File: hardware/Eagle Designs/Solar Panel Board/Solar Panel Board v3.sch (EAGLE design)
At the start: 44 parts, among them J1 MOLEX_503763-0291MOLEX_503763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, J2 MOLEX_503763-0491MOLEX_503763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, J3 MOLEX_503763-0291MOLEX_503763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, U1 TMP36GSZ, U2 INA219BIDR

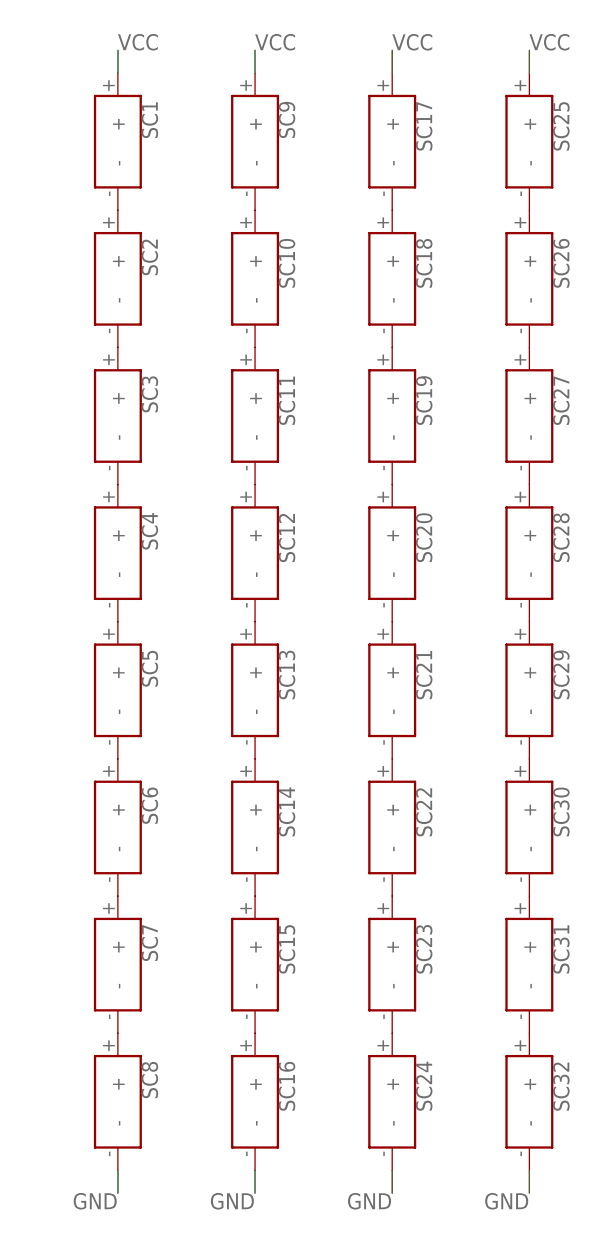
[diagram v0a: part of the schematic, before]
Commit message: Updated antenna and solar panel boards.
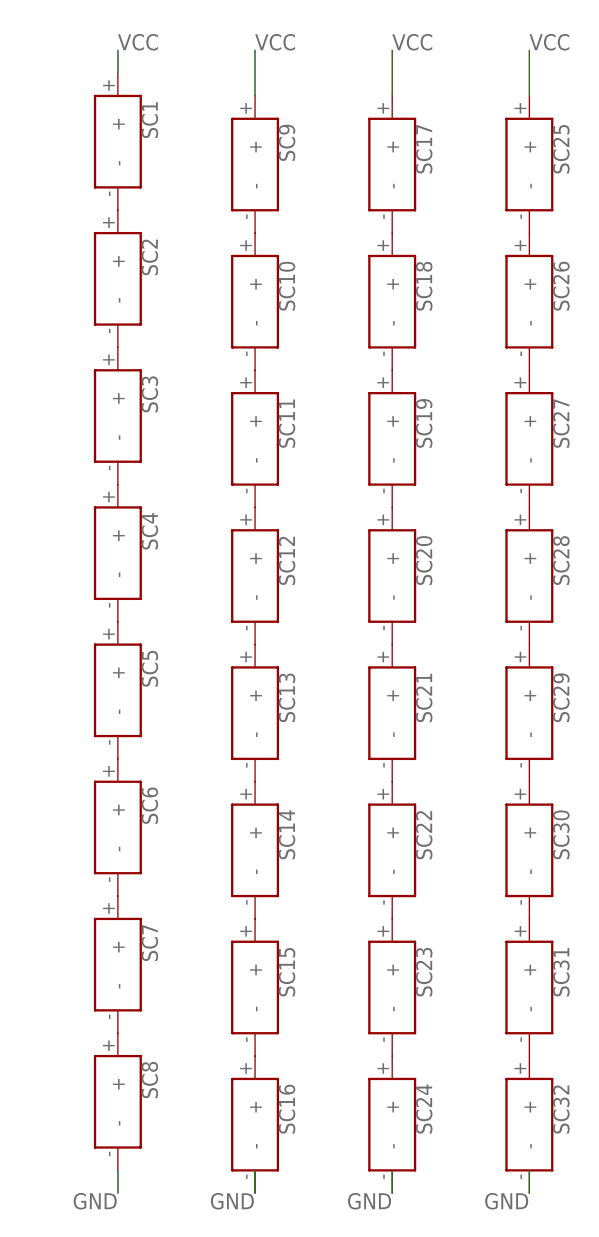
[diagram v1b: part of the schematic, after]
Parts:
- SC1, SC10, SC11, SC12, SC13, SC14, SC15, SC16, SC17, SC18, SC19, SC2, SC20, SC21, SC22, SC23, SC24, SC25, SC26, SC27, SC28, SC29, SC3, SC30, SC31, SC32, SC4, SC5, SC6, SC7, SC8, SC9: device KXOB25-05X3F:KXOB25-05X3F -> untitled:KXOB25-05X3F
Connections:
- removed net N$12 (its old number): SC12.-, SC13.+
- removed net N$14 (its old number): SC14.-, SC15.+
- removed net N$19 (its old number): SC20.-, SC21.+
- removed net N$26: SC28.-, SC29.+
- removed net N$28: SC30.-, SC31.+
- removed net N$5 (its old number): SC4.-, SC5.+
- removed net N$7 (its old number): SC6.-, SC7.+
- new net N$15: SC20.-, SC21.+, SC22.-, SC23.+
- new net N$3: SC4.-, SC5.+, SC6.-, SC7.+
- new net N$9: SC12.-, SC13.+, SC14.-, SC15.+
- net N$21: now also SC28.-, SC29.+, SC30.-, SC31.+; no longer SC22.-, SC23.+
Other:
- moved on the sheet: SC10, SC11, SC12, SC13, SC14, SC15, SC16, SC17, SC18, SC19, SC20, SC21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
